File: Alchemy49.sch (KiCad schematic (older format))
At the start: 205 parts, among them J1 USB_B_Micro, J2 Conn_01x05_Female, Q1 2N7002E, SW1 ESC-1.5U, SW10 O-1U, SW11 P-1U, SW12 BACK-1.5U, SW13 DEL-1U, SW14 TAB-1.75U, SW15 A-1U, SW16 S-1U, SW17 D-1U, SW18 F-1U, SW19 G-1U, SW2 Q-1U, SW20 H-1U, SW21 J-1U, SW22 K-1U, SW23 L-1U, SW24 ENTER-2.25U, SW25 PGUP-1U, SW26 SHIFT-2U, SW27 Z-1U, SW28 X-1U, SW29 C-1U, SW3 W-1U, SW30 V-1U, SW31 B-1U, SW32 N-1U, SW33 M-1U, SW34 COM-1U, SW35 PER-1U, SW36 SLASH-1U, SW37 UP-1U, SW38 PGDN-1U, SW39 CTRL1-1U, SW4 E-1U, SW40 WIN-1U, SW41 ALT-1U, SW42 FN1-1U, SW43 SPACE-2.75U, SW44 SHIFT-2.25U, SW45 FN2-1U, SW46 CTRL2-1U, SW47 LEFT-1U, SW48 DOWN-1U, SW49 RIGHT-1U, SW5 R-1U, SW6 T-1U, SW7 Y-1U, SW8 U-1U, SW9 I-1U

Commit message: Prototype Adjustments
* Added working KBFirmware config and hex files.
* Added example AVRDUDESS screenshot
* Added datasheet and part numbers to sch
* Adjusted pcb outlin and holes
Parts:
- removed H1, H2: MountingHole_Pad, MountingHole:MountingHole_3.5mm_Pad_Via, symbol Mechanical:MountingHole_Pad
- B1: Field4 XXX-00000 -> (none)
- D1, D10, D11, D12, D13, D14, D15, D16, D17, D18, D19, D2, D20, D21, D22, D23, D24, D25, D26, D27, D28, D29, D3, D30, D31, D32, D33, D34, D35, D36, D37, D38, D39, D4, D40, D41, D42, D43, D44, D45, D46, D47, D48, D49, D5, D6, D7, D8, D9: Field4 (none) -> C14538
- J1: Field4 (none) -> C46398
- Q1: Field4 (none) -> C193021
- R1, R10, R11, R12, R13, R14, R15, R16, R17, R18, R19, R2, R20, R21, R22, R23, R24, R25, R26, R27, R28, R29, R3, R30, R31, R32, R33, R34, R35, R36, R37, R38, R39, R4, R40, R41, R42, R43, R44, R45, R46, R47, R48, R49, R5, R6, R7, R8, R9: Field4 (none) -> C120043
- R50: Field4 (none) -> C120031
- R51: Field4 (none) -> C120262
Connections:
- no-connect marks 4 -> 2
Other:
- note removed: "Mounting Holes"

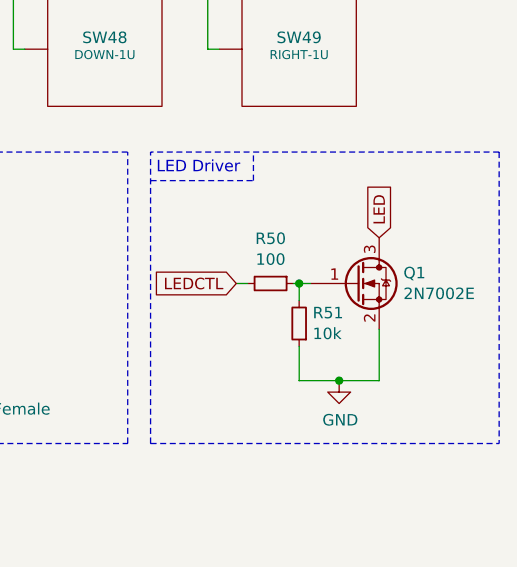
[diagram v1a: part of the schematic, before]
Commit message: Changed MOSFET to FDS6630A
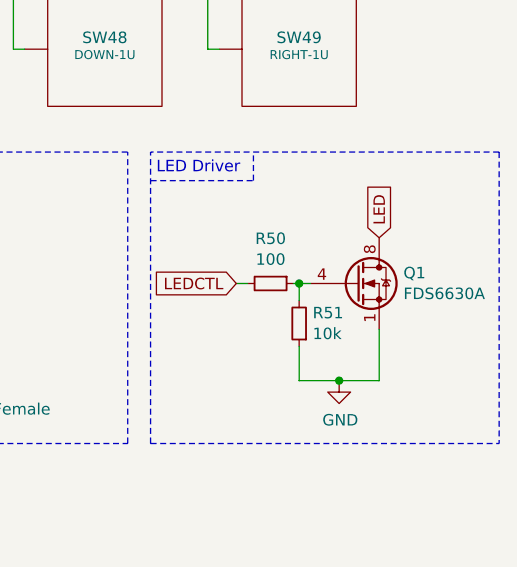
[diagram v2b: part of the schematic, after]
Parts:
- removed Q1: 2N7002E, Package_TO_SOT_SMD:SOT-23, symbol Transistor_FET:2N7002E
- added Q1: FDS6630A, Package_SO:SOIC-8_3.9x4.9mm_P1.27mm, symbol Transistor_FET:FDS6630A
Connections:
- net GND: now also Q1.1 (S), Q1.2 (S), Q1.3 (S)
- net LED: now also Q1.5 (D), Q1.6 (D), Q1.7 (D), Q1.8 (D)
- net at R50.1, R51.2: now also Q1.4 (G)
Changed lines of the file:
@@
 Wire Wire Line
 	9700 6475 9700 6575
-$Comp
-L Transistor_FET:2N7002E Q1
-U 1 1 5DC7DA73
-P 12775 5950
-F 0 "Q1" H 12981 5996 50  0000 L CNN
-F 1 "2N7002E" H 12981 5905 50  0000 L CNN
-F 2 "Package_TO_SOT_SMD:SOT-23" H 12975 5875 50  0001 L CIN
-F 3 "https://datasheet.lcsc.com/szlcsc/1811021222_AnBon-2N7002E_C193021.pdf" H 12775 5950 50  0001 L CNN
-F 4 "C193021" H 12775 5950 50  0001 C CNN "Field4"
-	1    12775 5950
-	1    0    0    -1
-$EndComp
 Wire Notes Line
 	9275 6650 11775 6650
@@
 Wire Wire Line
 	8500 6950 8600 6950
+$Comp
+L Transistor_FET:FDS6630A Q1
+U 1 1 5E51C3FE
+P 12775 5950
+F 0 "Q1" H 12981 5996 50  0000 L CNN
+F 1 "FDS6630A" H 12981 5905 50  0000 L CNN
+F 2 "Package_SO:SOIC-8_3.9x4.9mm_P1.27mm" H 12975 5850 50  0001 L CNN
+F 3 "http://www.onsemi.com/pub/Collateral/FDS6630A-D.pdf" H 12675 5950 50  0001 L CNN
+	1    12775 5950
+	1    0    0    -1
+$EndComp
 $EndSCHEMATC

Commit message: flipped the leds around the correct way
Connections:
- net VCC: now also LED1.A, LED10.A, LED11.A, LED12.A, LED13.A, LED14.A, LED15.A, LED16.A, LED17.A, LED18.A, LED19.A, LED2.A, LED20.A, LED21.A, LED22.A, LED23.A, LED24.A, LED25.A, LED26.A, LED27.A, LED28.A, LED29.A, LED3.A, LED30.A, LED31.A, LED32.A, LED33.A, LED34.A, LED35.A, LED36.A, LED37.A, LED38.A, LED39.A, LED4.A, LED40.A, LED41.A, LED42.A, LED43.A, LED44.A, LED45.A, LED46.A, LED47.A, LED48.A, LED49.A, LED5.A, LED6.A, LED7.A, LED8.A, LED9.A; no longer LED1.K, LED10.K, LED11.K, LED12.K, LED13.K, LED14.K, LED15.K, LED16.K, LED17.K, LED18.K, LED19.K, LED2.K, LED20.K, LED21.K, LED22.K, LED23.K, LED24.K, LED25.K, LED26.K, LED27.K, LED28.K, LED29.K, LED3.K, LED30.K, LED31.K, LED32.K, LED33.K, LED34.K, LED35.K, LED36.K, LED37.K, LED38.K, LED39.K, LED4.K, LED40.K, LED41.K, LED42.K, LED43.K, LED44.K, LED45.K, LED46.K, LED47.K, LED48.K, LED49.K, LED5.K, LED6.K, LED7.K, LED8.K, LED9.K
- net at R1.1: now also LED1.K; no longer LED1.A
- net at R2.1: now also LED2.K; no longer LED2.A
- net at R3.1: now also LED3.K; no longer LED3.A
- net at R4.1: now also LED4.K; no longer LED4.A
- net at R5.1: now also LED5.K; no longer LED5.A
- net at R6.1: now also LED6.K; no longer LED6.A
- net at R7.1: now also LED7.K; no longer LED7.A
- net at R8.1: now also LED8.K; no longer LED8.A
- net at R9.1: now also LED9.K; no longer LED9.A
- net at R10.1: now also LED10.K; no longer LED10.A
- net at R11.1: now also LED11.K; no longer LED11.A
- net at R12.1: now also LED12.K; no longer LED12.A
- net at R13.1: now also LED13.K; no longer LED13.A
- net at R14.1: now also LED14.K; no longer LED14.A
- net at R15.1: now also LED15.K; no longer LED15.A
- net at R16.1: now also LED16.K; no longer LED16.A
- net at R17.1: now also LED17.K; no longer LED17.A
- net at R18.1: now also LED18.K; no longer LED18.A
- net at R19.1: now also LED19.K; no longer LED19.A
- net at R20.1: now also LED20.K; no longer LED20.A
- net at R21.1: now also LED21.K; no longer LED21.A
- net at R22.1: now also LED22.K; no longer LED22.A
- net at R23.1: now also LED23.K; no longer LED23.A
- net at R24.1: now also LED24.K; no longer LED24.A
- net at R25.1: now also LED25.K; no longer LED25.A
- net at R26.1: now also LED26.K; no longer LED26.A
- net at R27.1: now also LED27.K; no longer LED27.A
- net at R28.1: now also LED28.K; no longer LED28.A
- net at R29.1: now also LED29.K; no longer LED29.A
- net at R30.1: now also LED30.K; no longer LED30.A
- net at R31.1: now also LED31.K; no longer LED31.A
- net at R32.1: now also LED32.K; no longer LED32.A
- net at R33.1: now also LED33.K; no longer LED33.A
- net at R34.1: now also LED34.K; no longer LED34.A
- net at R35.1: now also LED35.K; no longer LED35.A
- net at R36.1: now also LED36.K; no longer LED36.A
- net at R37.1: now also LED37.K; no longer LED37.A
- net at R38.1: now also LED38.K; no longer LED38.A
- net at R39.1: now also LED39.K; no longer LED39.A
- net at R40.1: now also LED40.K; no longer LED40.A
- net at R41.1: now also LED41.K; no longer LED41.A
- net at R42.1: now also LED42.K; no longer LED42.A
- net at R43.1: now also LED43.K; no longer LED43.A
- net at R44.1: now also LED44.K; no longer LED44.A
- net at R45.1: now also LED45.K; no longer LED45.A
- net at R46.1: now also LED46.K; no longer LED46.A
- net at R47.1: now also LED47.K; no longer LED47.A
- net at R48.1: now also LED48.K; no longer LED48.A
- net at R49.1: now also LED49.K; no longer LED49.A

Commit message: Changed MOSFET to AO3402, Removed 3D models from display
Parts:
- Q1: value FDS6630A -> AO3402A; footprint Package_SO:SOIC-8_3.9x4.9mm_P1.27mm -> Package_TO_SOT_SMD:SOT-23; symbol Transistor_FET:FDS6630A -> Transistor_FET:DMG3402L
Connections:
- net GND: no longer Q1.1 (S), Q1.3 (S)
- net LED: now also Q1.3 (D); no longer Q1.5 (D), Q1.6 (D), Q1.7 (D), Q1.8 (D)
- net SHLD: now reaches J1.6 (Shield), J2.5 (Pin_5)
- net at R50.1, R51.2: now also Q1.1 (G); no longer Q1.4 (G)
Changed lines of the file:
@@
 EESchema Schematic File Version 4
-LIBS:Alchemy49-cache
 EELAYER 30 0
 EELAYER END
@@
 	8500 6950 8600 6950
 $Comp
-L Transistor_FET:FDS6630A Q1
+L Transistor_FET:DMG3402L Q1
 U 1 1 5E51C3FE
 P 12775 5950
 F 0 "Q1" H 12981 5996 50  0000 L CNN
-F 1 "FDS6630A" H 12981 5905 50  0000 L CNN
-F 2 "Package_SO:SOIC-8_3.9x4.9mm_P1.27mm" H 12975 5850 50  0001 L CNN
-F 3 "http://www.onsemi.com/pub/Collateral/FDS6630A-D.pdf" H 12675 5950 50  0001 L CNN
+F 1 "AO3402A" H 12981 5905 50  0000 L CNN
+F 2 "Package_TO_SOT_SMD:SOT-23" H 12975 5850 50  0001 L CNN
+F 3 "https://datasheet.lcsc.com/szlcsc/1808131821_Alpha-Omega-Semicon-AO3402_C14385.pdf" H 12675 5950 50  0001 L CNN
 	1    12775 5950
 	1    0    0    -1
@@
 Wire Wire Line
 	6525 6300 6525 6725
+Text GLabel 10525 6575 2    30   Input ~ 0
+SHLD
+Wire Wire Line
+	10525 6575 10450 6575
+Connection ~ 10450 6575
 $EndSCHEMATC

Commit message: New Graphics
Added newest gerbers and graphics. Also added LCSC field to sch
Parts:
- D1, D10, D11, D12, D13, D14, D15, D16, D17, D18, D19, D2, D20, D21, D22, D23, D24, D25, D26, D27, D28, D29, D3, D30, D31, D32, D33, D34, D35, D36, D37, D38, D39, D4, D40, D41, D42, D43, D44, D45, D46, D47, D48, D49, D5, D6, D7, D8, D9: Field4 C14538 -> (none); LCSC (none) -> C14538
- J1: Field4 C46398 -> (none); LCSC (none) -> C46398
- LED1, LED10, LED11, LED12, LED13, LED14, LED15, LED16, LED17, LED18, LED19, LED2, LED20, LED21, LED22, LED23, LED24, LED25, LED26, LED27, LED28, LED29, LED3, LED30, LED31, LED32, LED33, LED34, LED35, LED36, LED37, LED38, LED39, LED4, LED40, LED41, LED42, LED43, LED44, LED45, LED46, LED47, LED48, LED49, LED5, LED6, LED7, LED8, LED9: LCSC (none) -> C268275
- Q1: LCSC (none) -> C351406
- R1, R10, R11, R12, R13, R14, R15, R16, R17, R18, R19, R2, R20, R21, R22, R23, R24, R25, R26, R27, R28, R29, R3, R30, R31, R32, R33, R34, R35, R36, R37, R38, R39, R4, R40, R41, R42, R43, R44, R45, R46, R47, R48, R49, R5, R6, R7, R8, R9: Field4 C120043 -> (none); LCSC (none) -> C119858
- R50: Field4 C120031 -> (none); LCSC (none) -> C119846
- R51: Field4 C120262 -> (none); LCSC (none) -> C119894
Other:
- moved on the sheet: J1, J2, R50, R51

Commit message: Changed to combination THT and surfacemount for the diodes
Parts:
- D1, D10, D11, D12, D13, D14, D15, D16, D17, D18, D19, D2, D20, D21, D22, D23, D24, D25, D26, D27, D28, D29, D3, D30, D31, D32, D33, D34, D35, D36, D37, D38, D39, D4, D40, D41, D42, D43, D44, D45, D46, D47, D48, D49, D5, D6, D7, D8, D9: footprint AcheronLibrary_COM:D_THT_7.62mm -> AcheronLibrary_COM:D_THT_7.62mm_SOD-123
- R1, R10, R11, R12, R13, R14, R15, R16, R17, R18, R19, R2, R20, R21, R22, R23, R24, R25, R26, R27, R28, R29, R3, R30, R31, R32, R33, R34, R35, R36, R37, R38, R39, R4, R40, R41, R42, R43, R44, R45, R46, R47, R48, R49, R5, R50, R51, R6, R7, R8, R9: footprint AcheronLibrary_COM:R_THT_5.08mm_Horizontal -> Alchemy49:R_THT_5.08mm_SMD_1206
